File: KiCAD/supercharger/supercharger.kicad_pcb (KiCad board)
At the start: 2 copper layers, 53.5 x 9.8 mm, 12 parts, among them J2 BAT, J3 CALC, J4 UJC-H-G-SMT-1-P6-TR

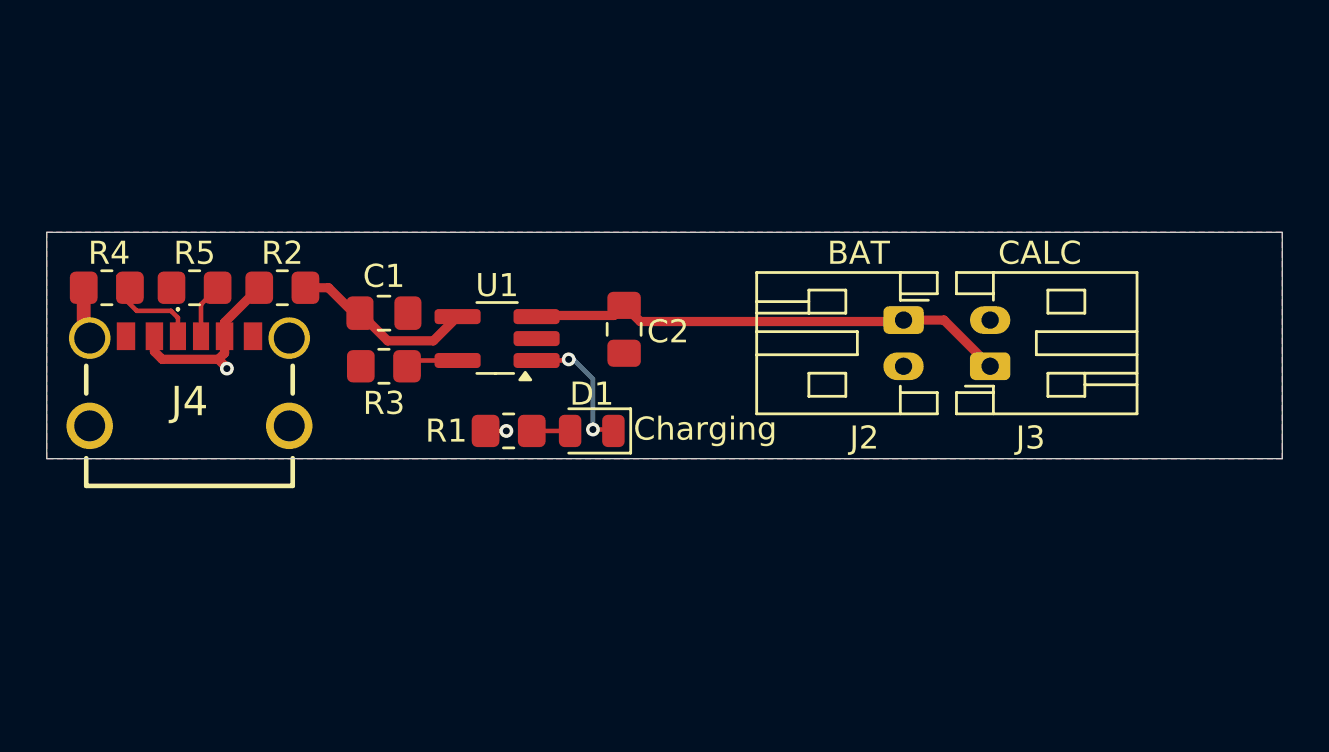
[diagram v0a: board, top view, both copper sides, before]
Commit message: README.md update
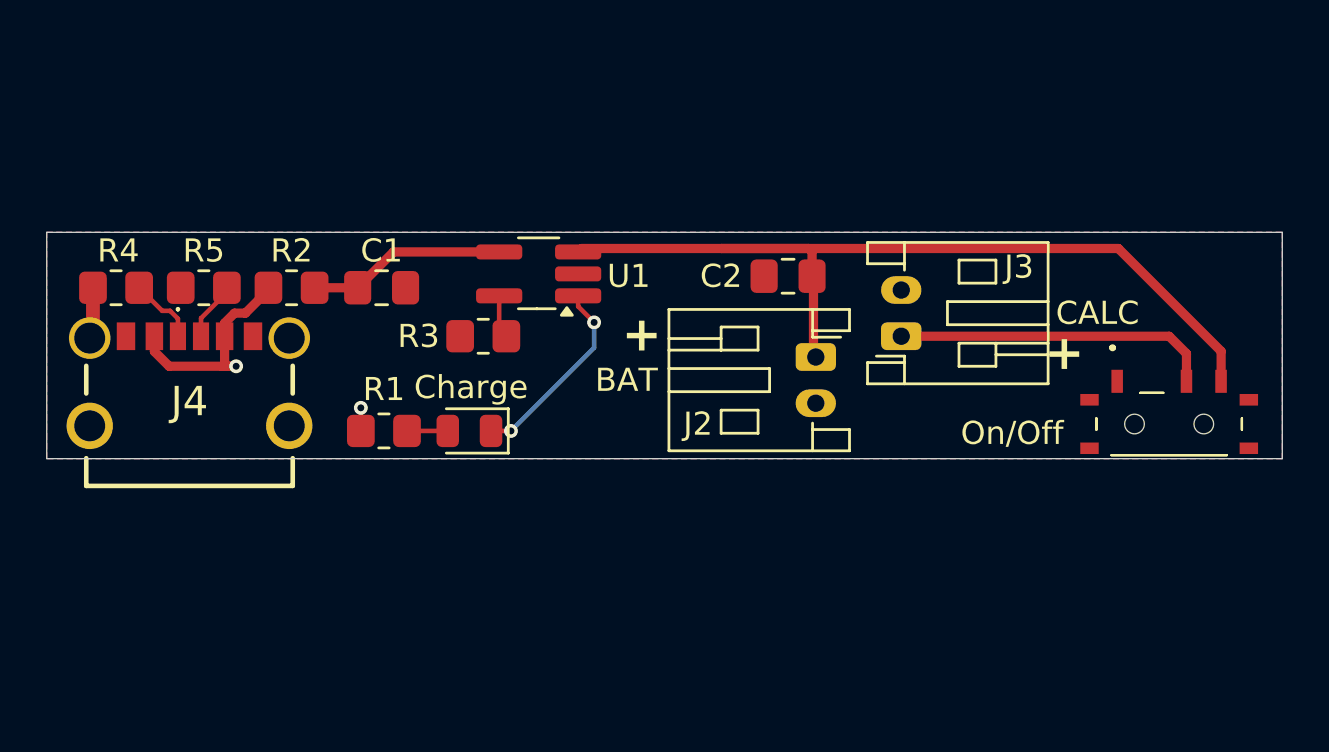
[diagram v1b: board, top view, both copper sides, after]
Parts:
- added S1: On/Off, EC-parts:MSK12C02, F.Cu at (138.6, 98.5)
- moved C2 7.46 mm to (122.1, 92.1), turned to 0 degrees
- moved R1 5.40 mm to (104.6, 98.8)
- moved D1 5.30 mm to (108.3, 98.8)
- moved R3 4.49 mm to (108.9, 94.7)
- moved J2 4.12 mm to (123.3, 95.6)
- moved J3 4.06 mm to (127.0, 94.7)
- moved U1 3.33 mm to (111.3, 92.0)
- moved C1 1.10 mm to (104.5, 92.6)
- moved R4 0.40 mm to (93.0, 92.6)
- moved R2 0.40 mm to (100.6, 92.6)
- moved R5 0.40 mm to (96.8, 92.6)
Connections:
- J3 pad 1: Net-(J2-Pin_1) -> Net-(J3-Pin_1)
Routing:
- net Net-(J2-Pin_1): track 21.0 -> 39.3 mm
- net Net-(J3-Pin_1): track 0.00 -> 13.4 mm
- net Net-(D1-K): track 5.91 -> 8.49 mm
- net +5V: track 8.86 -> 10.6 mm
- net Net-(J4-CC1): track 4.54 -> 3.00 mm
- net Net-(U1-VCC): track 7.98 -> 8.63 mm
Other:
- board text added: "+"
- board text added: "Charge"
- board text added: "PowerStation 2026"
- board text added: "Supercharger v1.0"
- board text removed: "Charging"

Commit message: Add buttons + charge display. Still need better/smaller connectors
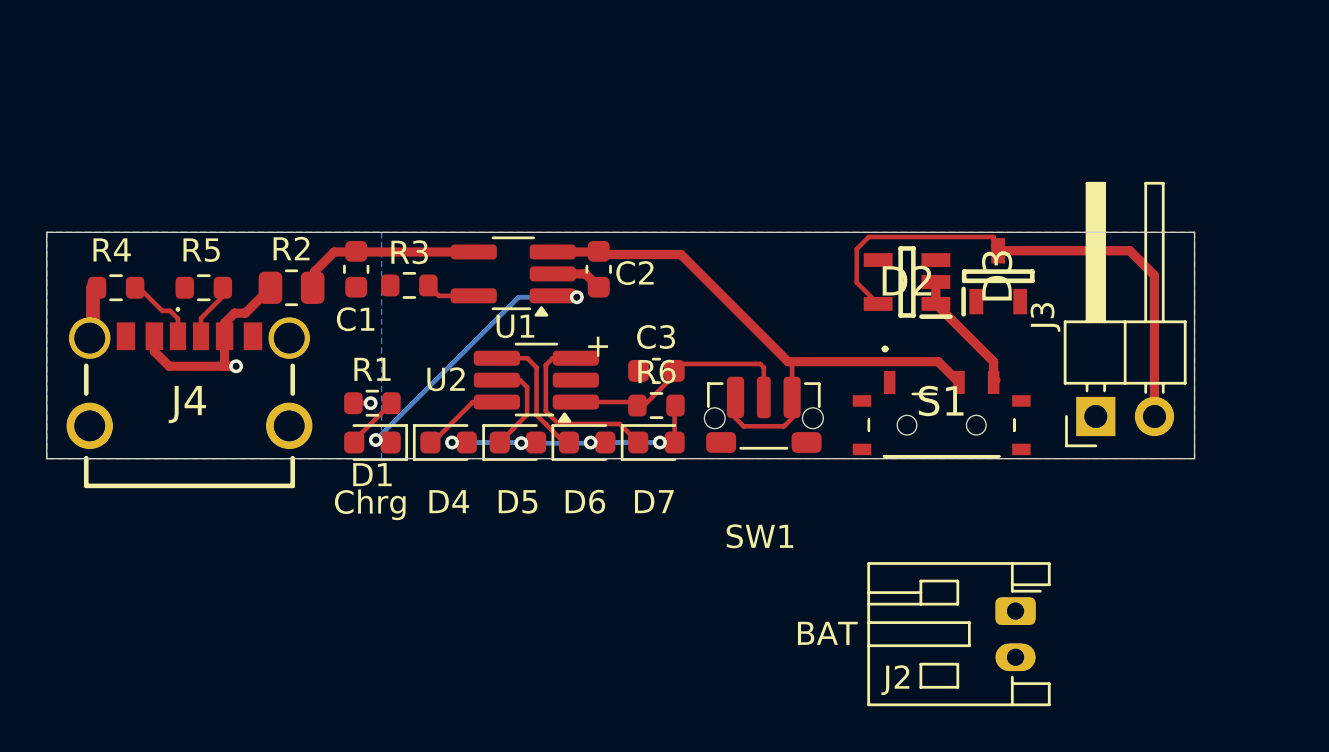
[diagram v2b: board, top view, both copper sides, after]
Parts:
- added C3: 1u, Capacitor_SMD:C_0603_1608Metric, F.Cu at (116.4, 96.2)
- added D2: MAX40203AUK+, EC-parts:SOT95P280X145-5N, F.Cu at (127.2, 92.3)
- added D3: MMBZ5231B-HE3-08, EC-parts:SOT95P248X115-3N, F.Cu at (131.2, 92.1)
- added D4: LED, LED_SMD:LED_0603_1608Metric, F.Cu at (107.4, 99.3)
- added D5: LED, LED_SMD:LED_0603_1608Metric, F.Cu at (110.4, 99.3)
- added D6: LED, LED_SMD:LED_0603_1608Metric, F.Cu at (113.4, 99.3)
- added D7: LED, LED_SMD:LED_0603_1608Metric, F.Cu at (116.4, 99.3)
- added R6: 330R, Resistor_SMD:R_0603_1608Metric, F.Cu at (116.4, 97.7)
- added SW1: SW_SPST, Button_Switch_SMD:SW_Push_1P1T-MP_NO_Horizontal_Alps_SKRTLAE010, F.Cu at (121.0, 98.2)
- added U2: ~, Package_TO_SOT_SMD:TSOT-23-6_HandSoldering, F.Cu at (111.2, 96.6)
- C1, C2: footprint Capacitor_SMD:C_0805_2012Metric_Pad1.18x1.45mm_HandSolder -> Capacitor_SMD:C_0603_1608Metric
- D1: footprint LED_SMD:LED_0805_2012Metric -> LED_SMD:LED_0603_1608Metric
- J3: footprint Connector_JST:JST_PH_S2B-PH-K_1x02_P2.00mm_Horizontal -> Connector_PinHeader_2.54mm:PinHeader_1x02_P2.54mm_Horizontal
- R1, R3, R4, R5: footprint Resistor_SMD:R_0805_2012Metric_Pad1.20x1.40mm_HandSolder -> Resistor_SMD:R_0603_1608Metric
- R2: footprint Resistor_SMD:R_0805_2012Metric_Pad1.20x1.40mm_HandSolder -> Resistor_SMD:R_0805_2012Metric
- S1: value On/Off -> MSK12C02
- moved J2 14.0 mm to (131.9, 106.6)
- moved S1 9.85 mm to (128.8, 98.5)
- moved J3 9.11 mm to (135.4, 98.2)
- moved C2 8.21 mm to (113.9, 91.8), turned to 90 degrees
- moved D1 4.23 mm to (104.1, 99.3)
- moved R3 3.88 mm to (105.7, 92.5)
- moved C1 1.36 mm to (103.4, 91.8), turned to -90 degrees
- moved R1 1.30 mm to (104.1, 97.6)
- moved U1 1.10 mm to (110.2, 92.0)
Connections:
- J3 pad 1: Net-(J3-Pin_1) -> GND
- J3 pad 2: GND -> Net-(D2-OUT)
- S1 pad B1: Net-(J3-Pin_1) -> Net-(J2-Pin_1)
- S1 pad C1: Net-(J2-Pin_1) -> Net-(D2-GND)
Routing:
- net Net-(D2-OUT): track 0.00 -> 22.9 mm
- net Net-(J3-Pin_1): track 13.4 -> 0.00 mm
- net Net-(J2-Pin_1): track 39.3 -> 26.1 mm
- net Net-(D4-A): track 0.00 -> 13.2 mm, vias 0 -> 4
- net Net-(SW1-B): track 0.00 -> 10.4 mm
- net Net-(D7-K): track 0.00 -> 7.98 mm
- net Net-(D6-K): track 0.00 -> 5.84 mm
- net Net-(D2-GND): track 0.00 -> 5.53 mm
- net Net-(D1-K): track 8.49 -> 13.0 mm
- net Net-(D5-K): track 0.00 -> 4.32 mm
- net Net-(D4-K): track 0.00 -> 3.60 mm
- net GND: track 2.26 -> 4.54 mm
- net Net-(U1-VCC): track 8.63 -> 7.94 mm
- net Net-(D1-A): track 1.76 -> 2.37 mm
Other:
- board size 53.5 x 9.8 mm -> 49.7 x 9.8 mm
- board text added: "Chrg"
- board text removed: "Charge"

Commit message: Rearrange components, add the elusive JST 1.25mm 2-pole connector (DIY).
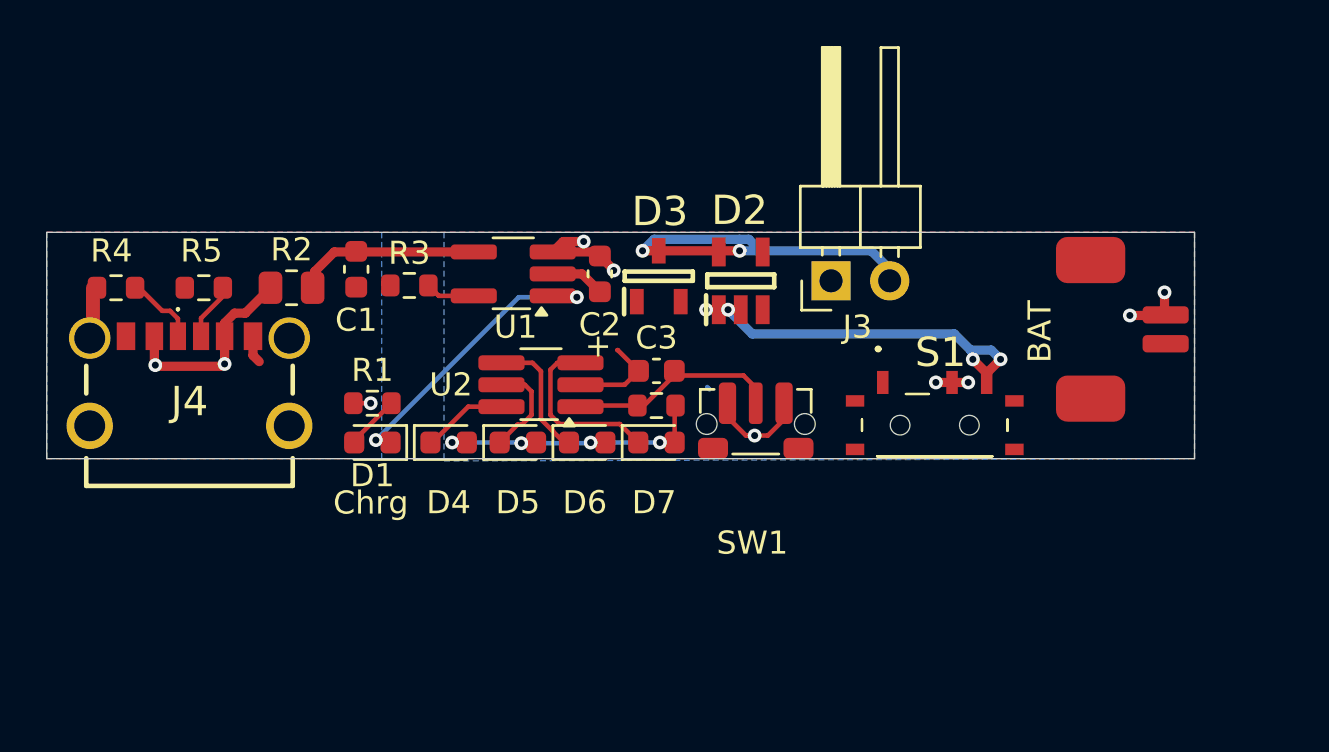
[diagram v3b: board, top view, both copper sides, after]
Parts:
- J2: footprint Connector_JST:JST_PH_S2B-PH-K_1x02_P2.00mm_Horizontal -> MFI_DIY_footprints:Connector JST PH 1.25mm horizontal
- moved D3 14.7 mm to (116.5, 92.1)
- moved J2 13.1 mm to (136.7, 94.4), turned to 90 degrees
- moved J3 12.9 mm to (124.0, 92.3)
- moved D2 7.20 mm to (120.0, 92.3), turned to 90 degrees
- moved SW1 0.43 mm to (120.7, 98.5)
- moved S1 0.30 mm to (128.4, 98.5)
- moved U2 0.28 mm to (111.4, 96.8)
- moved C2 0.21 mm to (114.0, 92.0)
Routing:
- net Net-(S1-COM): track 26.1 -> 12.9 mm, vias 0 -> 7
- net Net-(D2-GND): track 5.53 -> 18.2 mm, vias 0 -> 4
- net Net-(D2-OUT): track 22.9 -> 16.5 mm, vias 0 -> 2
- net GND: track 4.54 -> 9.67 mm
- net Net-(SW1-B): track 10.4 -> 8.14 mm
- net +5V: track 10.3 -> 9.20 mm, vias 2 -> 3
- added copper zone on B.Cu, net Net-(S1-COM)

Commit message: Move USB-C towards side by 1mm, tweak component placement, Add lid and PCB dummies
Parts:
- removed S1: MSK12C02, EC-parts:MSK12C02
- removed SW1: SW_SPST, Button_Switch_SMD:SW_Push_1P1T-MP_NO_Horizontal_Alps_SKRTLAE010
- added OnOff1: OnOff, EC-parts:MSK12C02, F.Cu at (128.4, 98.6)
- added State1: State, EC-parts:B3U3000PMB, F.Cu at (120.7, 98.8)
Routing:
- net Net-(OnOff1-COM): track 12.9 -> 9.73 mm
- net Net-(D2-GND): track 18.2 -> 19.3 mm
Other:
- board size 49.7 x 9.8 mm -> 49.7 x 10 mm

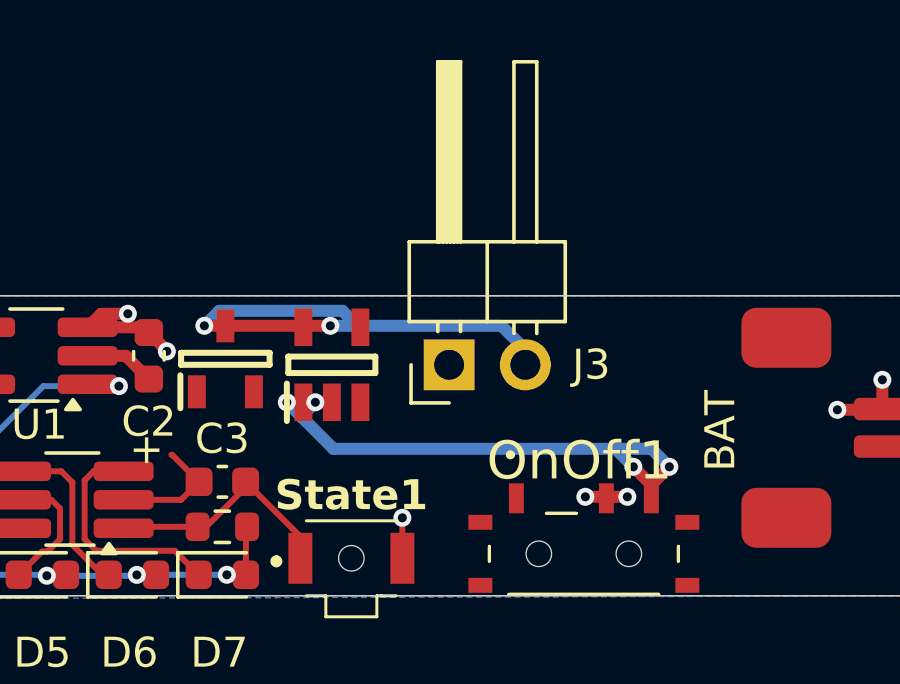
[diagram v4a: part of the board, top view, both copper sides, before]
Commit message: Update supercharger with wired interconnect to intercooler.
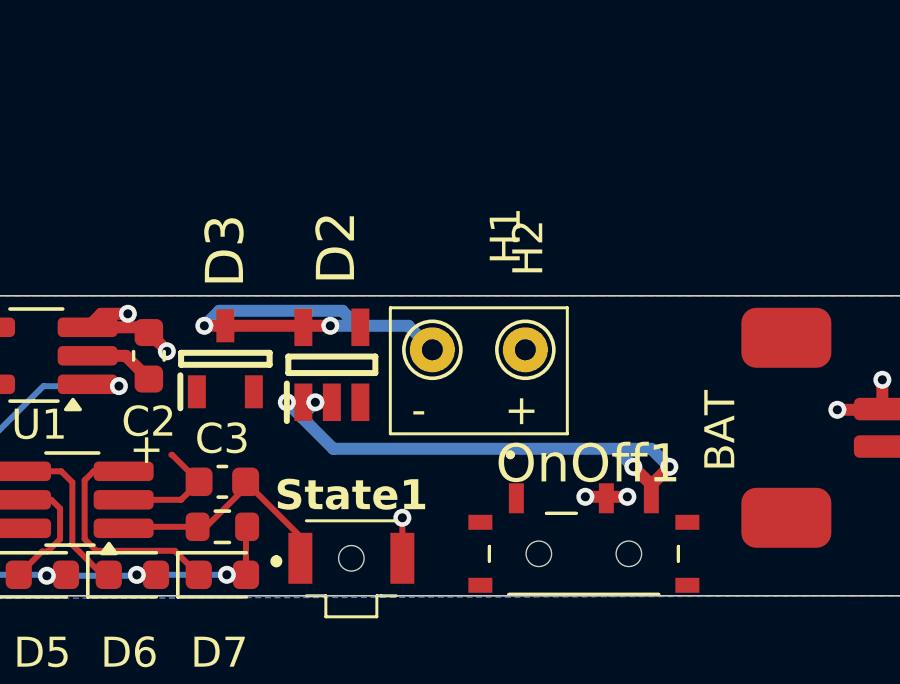
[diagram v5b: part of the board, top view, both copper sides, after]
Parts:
- removed J3: CALC, Connector_PinHeader_2.54mm:PinHeader_1x02_P2.54mm_Horizontal
- added H1: CALC, TestPoint:TestPoint_THTPad_D1.5mm_Drill0.7mm, F.Cu at (123.4, 91.8)
- added H2: CALC, TestPoint:TestPoint_THTPad_D1.5mm_Drill0.7mm, F.Cu at (126.5, 91.8)
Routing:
- net Net-(D2-OUT): track 16.5 -> 13.4 mm
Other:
- board text added: "-"

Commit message: v1.0: Bestilt hos JLCPCB 260626
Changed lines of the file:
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@@
 		(tags "capacitor")
 		(property "Reference" "C3"
-			(at 0 -1.43 0)
+			(at 0 -1.3 0)
 			(layer "F.SilkS")
 			(effects
@@
 		(tags "resistor")
 		(property "Reference" "R1"
-			(at 0 -1.43 0)
+			(at 0.1 4.4 0)
 			(layer "F.SilkS")
 			(effects
@@
 		(tags "Switch")
 		(property "Reference" "OnOff1"
-			(at 0.15 -3 0)
-			(layer "F.SilkS")
+			(at 0.15 -3.2 0)
+			(layer "F.SilkS" knockout)
 			(effects
 				(font
-					(size 1.27 1.27)
-					(thickness 0.254)
+					(size 1 1)
+					(thickness 0.1)
 				)
 			)
@@
 		(property "Reference" "State1"
 			(at 0 2.1 0)
-			(layer "F.SilkS")
+			(layer "F.SilkS" knockout)
 			(effects
 				(font
 					(size 1 1)
-					(thickness 0.2)
-					(bold yes)
+					(thickness 0.1)
 				)
 			)
@@
 		(tags "capacitor")
 		(property "Reference" "C2"
-			(at -2.2 0 180)
+			(at -2.1 -0.05 180)
 			(layer "F.SilkS")
 			(effects
@@
 	(gr_rect
 		(start 122 90.4)
-		(end 127.9 94.6)
+		(end 127.9 94.3)
 		(stroke
 			(width 0.1)
@@
 	)
 	(gr_text "Chrg"
-		(at 102.4 102.5 0)
+		(at 102.4 96.6 0)
 		(layer "F.SilkS" knockout)
 		(effects
@@
 	)
 	(gr_text "-"
-		(at 122.7 94.4 0)
+		(at 125.8 94.1 0)
 		(layer "F.SilkS")
 		(effects
@@
 	)
 	(gr_text "+"
-		(at 125.8 94.4 0)
+		(at 122.7 94.1 0)
 		(layer "F.SilkS")
 		(effects
@@
 		(layer "User.1")
 		(pts
-			(xy 139.7 90) (xy 123.9 90)
+			(xy 139.7 90) (xy 123.4 90)
 		)
 		(height 13.8)
-		(gr_text "15.8000 mm"
-			(at 131.8 75.05 0)
+		(gr_text "16.3000 mm"
+			(at 131.55 75.05 0)
 			(layer "User.1")
 			(effects
